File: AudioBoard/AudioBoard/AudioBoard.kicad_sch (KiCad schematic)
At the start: 0 parts

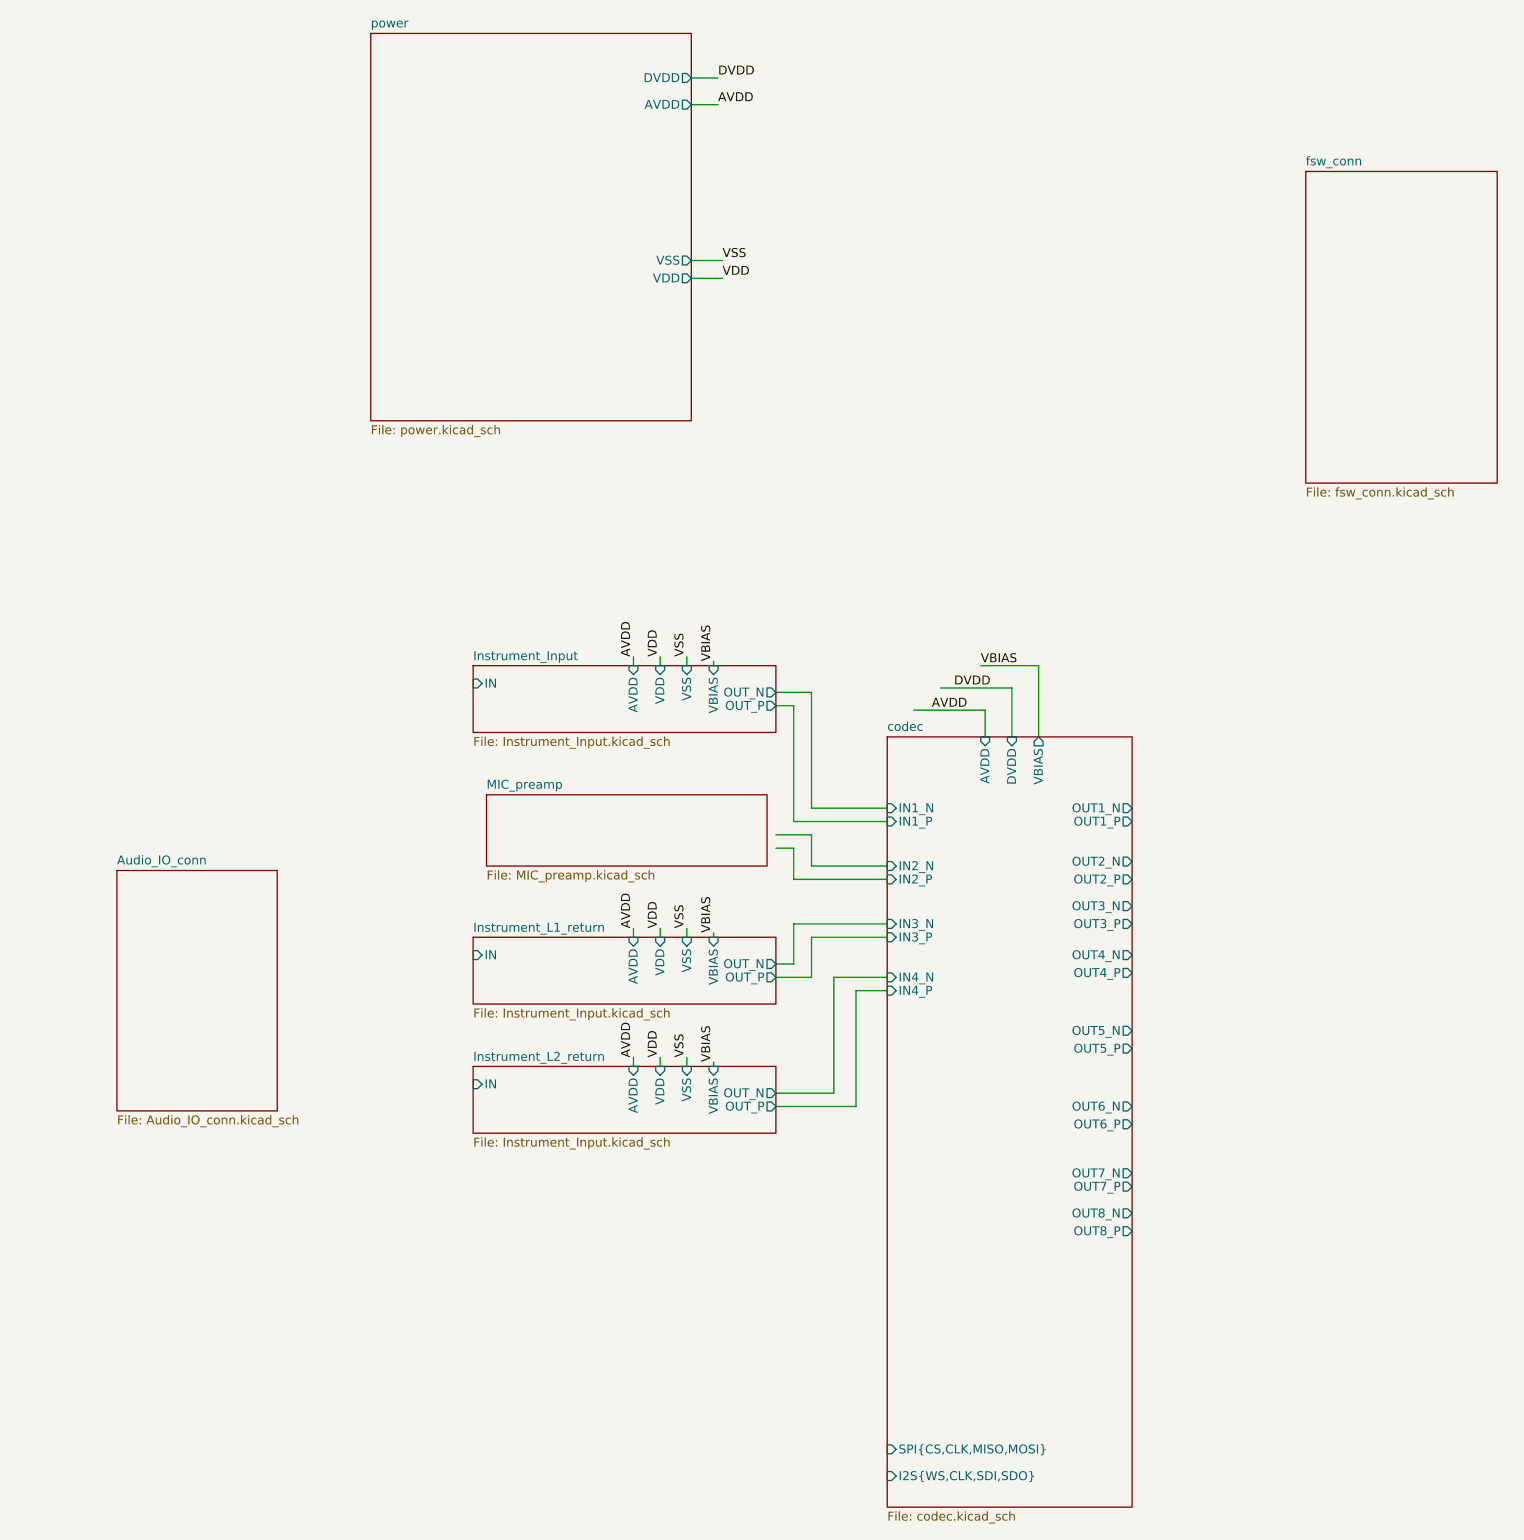
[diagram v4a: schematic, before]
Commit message: added xlr output stage
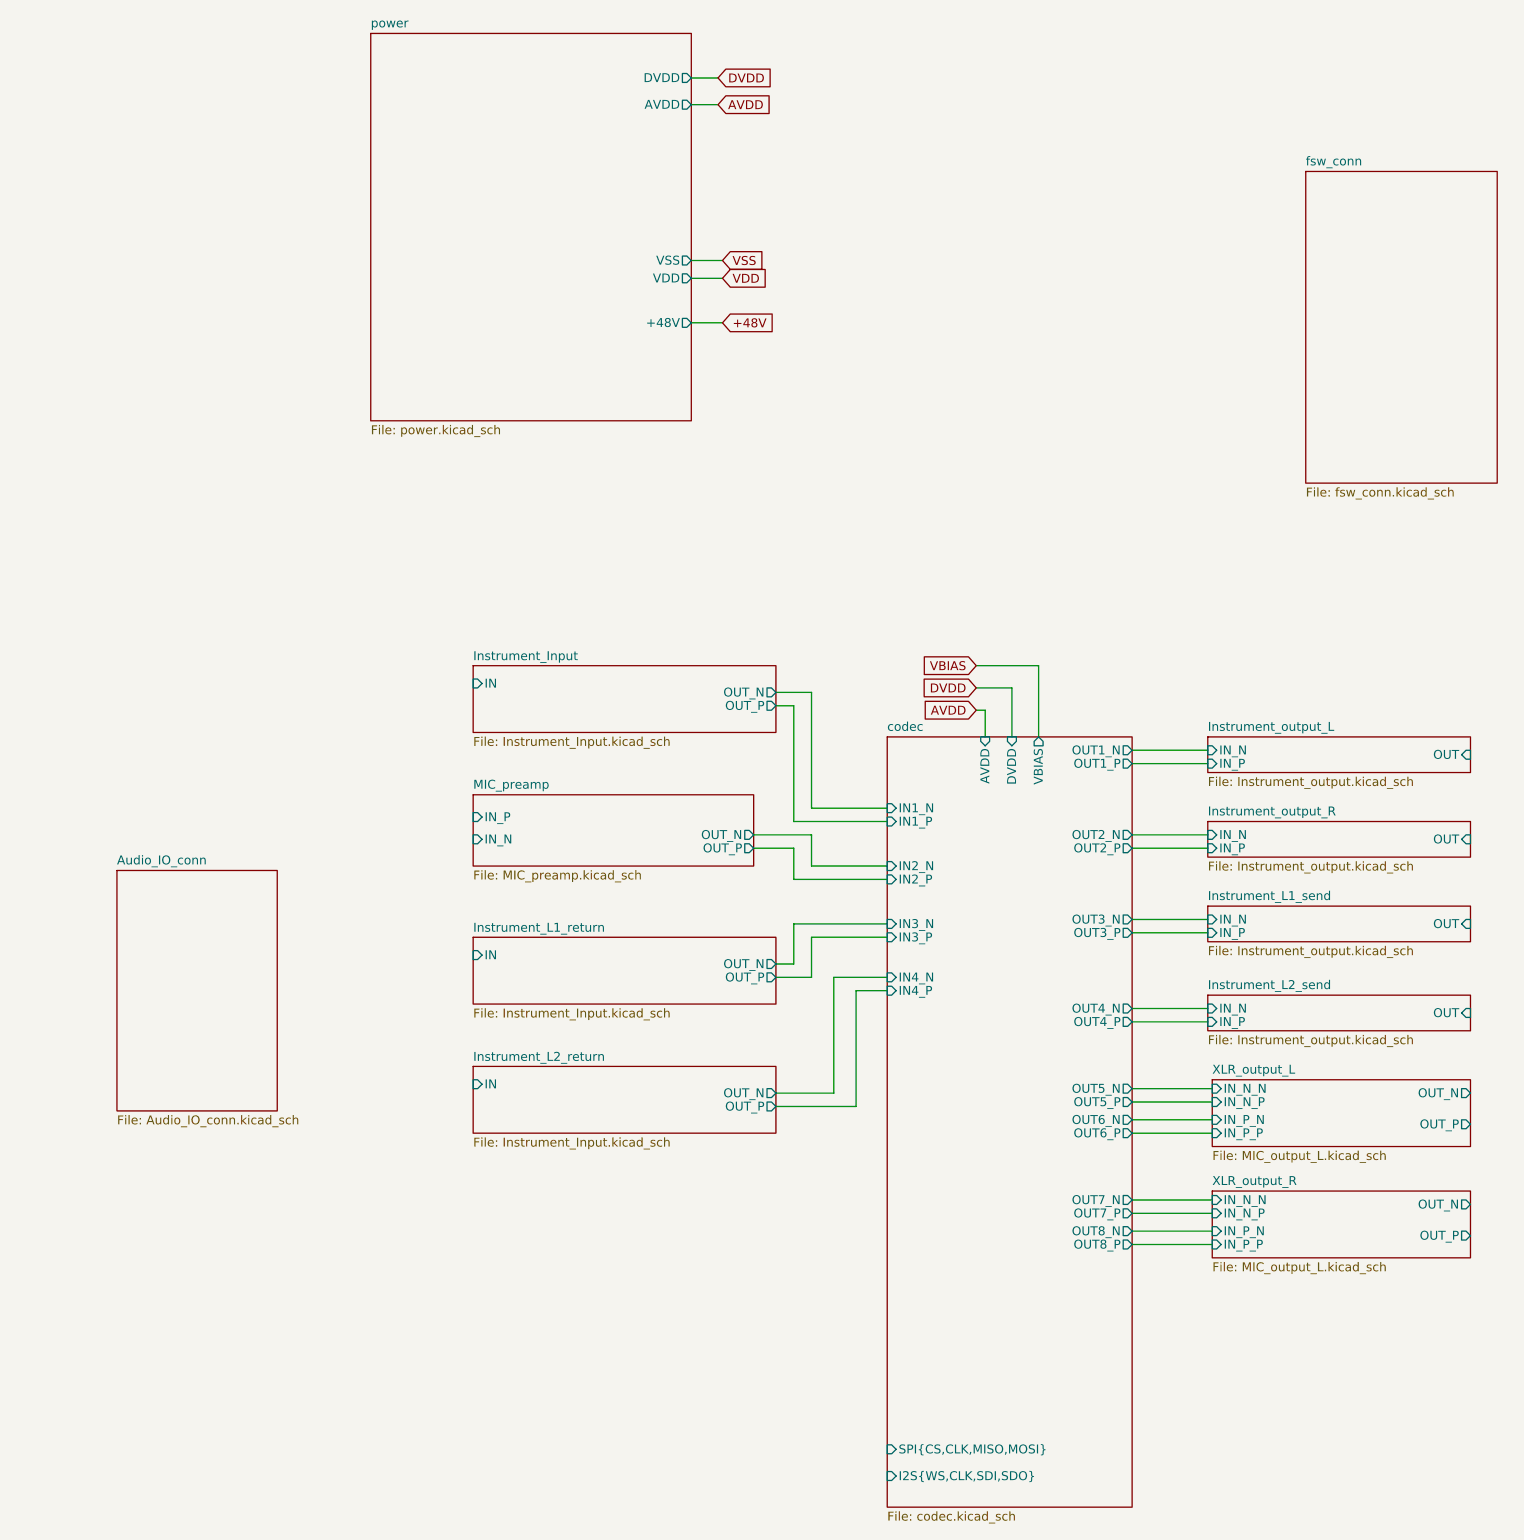
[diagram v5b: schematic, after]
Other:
- added sheet Instrument_L1_send (Instrument_output.kicad_sch)
- added sheet Instrument_L2_send (Instrument_output.kicad_sch)
- added sheet Instrument_output_L (Instrument_output.kicad_sch)
- added sheet Instrument_output_R (Instrument_output.kicad_sch)
- added sheet XLR_output_L (MIC_output_L.kicad_sch)
- added sheet XLR_output_R (MIC_output_L.kicad_sch)
- sheet Instrument_Input ports: added none; removed AVDD, VBIAS, VDD, VSS
- sheet Instrument_L1_return ports: added none; removed AVDD, VBIAS, VDD, VSS
- sheet Instrument_L2_return ports: added none; removed AVDD, VBIAS, VDD, VSS
- sheet MIC_preamp ports: added IN_N, IN_P, OUT_N, OUT_P; removed none
- sheet power ports: added +48V; removed none

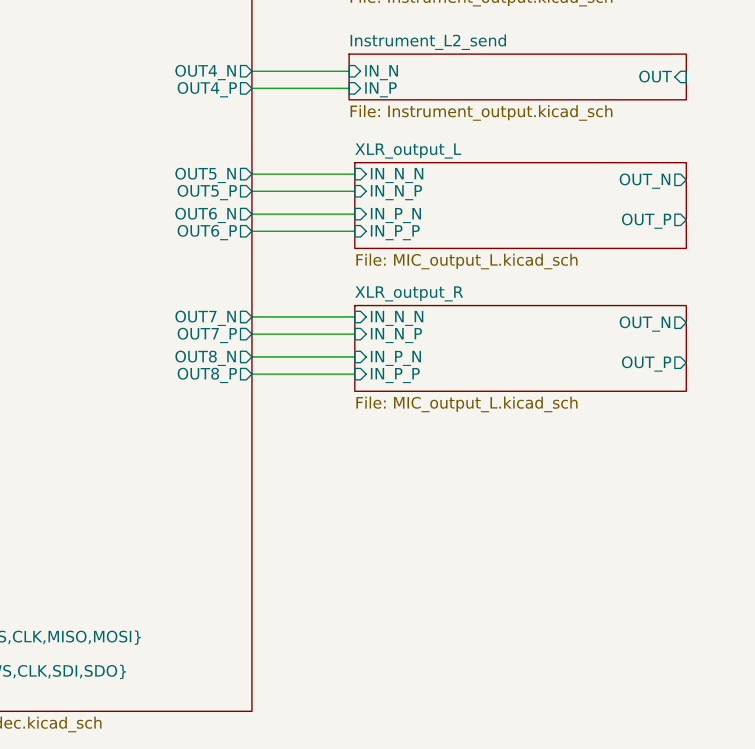
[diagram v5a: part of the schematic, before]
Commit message: added dxf file to pcb view
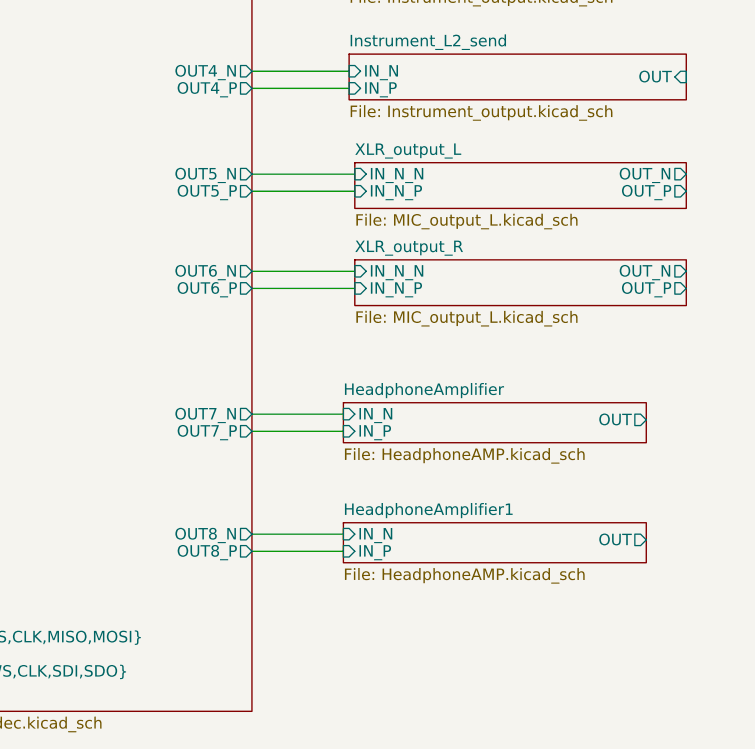
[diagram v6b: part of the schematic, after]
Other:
- added sheet HeadphoneAmplifier (HeadphoneAMP.kicad_sch)
- added sheet HeadphoneAmplifier1 (HeadphoneAMP.kicad_sch)
- sheet XLR_output_L ports: added none; removed IN_P_N, IN_P_P
- sheet XLR_output_R ports: added none; removed IN_P_N, IN_P_P
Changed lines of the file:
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@@
+	(wire
+		(pts
+			(xy 227.965 219.075) (xy 238.125 219.075)
+		)
+		(stroke
+			(width 0)
+			(type default)
+		)
+	)
 	(wire
 		(pts
@@
 	(wire
 		(pts
-			(xy 227.965 210.82) (xy 239.395 210.82)
-		)
-		(stroke
-			(width 0)
-			(type default)
-		)
-	)
-	(wire
-		(pts
 			(xy 179.705 152.4) (xy 193.04 152.4)
 		)
@@
 	(wire
 		(pts
-			(xy 227.965 208.28) (xy 239.395 208.28)
+			(xy 227.965 201.295) (xy 239.395 201.295)
 		)
 		(stroke
@@
 	(wire
 		(pts
+			(xy 227.965 203.2) (xy 239.395 203.2)
+		)
+		(stroke
+			(width 0)
+			(type default)
+		)
+	)
+	(wire
+		(pts
 			(xy 207.01 136.525) (xy 207.01 140.335)
 		)
@@
 	(wire
 		(pts
-			(xy 227.965 196.85) (xy 239.395 196.85)
-		)
-		(stroke
-			(width 0)
-			(type default)
-		)
-	)
-	(wire
-		(pts
 			(xy 193.04 167.005) (xy 179.705 167.005)
 		)
@@
 	(wire
 		(pts
+			(xy 227.965 217.17) (xy 238.125 217.17)
+		)
+		(stroke
+			(width 0)
+			(type default)
+		)
+	)
+	(wire
+		(pts
 			(xy 169.545 72.39) (xy 165.1 72.39)
 		)
@@
 	(wire
 		(pts
+			(xy 227.965 232.41) (xy 238.125 232.41)
+		)
+		(stroke
+			(width 0)
+			(type default)
+		)
+	)
+	(wire
+		(pts
 			(xy 227.965 180.975) (xy 238.76 180.975)
 		)
@@
 	(wire
 		(pts
-			(xy 239.395 194.945) (xy 227.965 194.945)
-		)
-		(stroke
-			(width 0)
-			(type default)
-		)
-	)
-	(wire
-		(pts
 			(xy 227.965 192.405) (xy 239.395 192.405)
 		)
@@
 	(wire
 		(pts
-			(xy 227.965 206.375) (xy 239.395 206.375)
+			(xy 227.965 230.505) (xy 238.125 230.505)
 		)
 		(stroke
@@
 		(pts
 			(xy 173.99 156.21) (xy 179.705 156.21)
-		)
-		(stroke
-			(width 0)
-			(type default)
-		)
-	)
-	(wire
-		(pts
-			(xy 227.965 212.725) (xy 239.395 212.725)
 		)
 		(stroke
@@
 	)
 	(sheet
+		(at 238.125 229.235)
+		(size 33.655 4.445)
+		(exclude_from_sim no)
+		(in_bom yes)
+		(on_board yes)
+		(dnp no)
+		(fields_autoplaced yes)
+		(stroke
+			(width 0.1524)
+			(type solid)
+		)
+		(fill
+			(color 0 0 0 0)
+		)
+		(property "Sheetname" "HeadphoneAmplifier1"
+			(at 238.125 228.5234 0)
+			(show_name no)
+			(do_not_autoplace no)
+			(effects
+				(font
+					(size 1.27 1.27)
+				)
+				(justify left bottom)
+			)
+		)
+		(property "Sheetfile" "HeadphoneAMP.kicad_sch"
+			(at 238.125 234.2646 0)
+			(show_name no)
+			(do_not_autoplace no)
+			(effects
+				(font
+					(size 1.27 1.27)
+				)
+				(justify left top)
+			)
+		)
+		(pin "IN_N" input
+			(at 238.125 230.505 180)
+			(effects
+				(font
+					(size 1.27 1.27)
+				)
+				(justify left)
+			)
+		)
+		(pin "IN_P" input
+			(at 238.125 232.41 180)
+			(effects
+				(font
+					(size 1.27 1.27)
+				)
+				(justify left)
+			)
+		)
+		(pin "OUT" output
+			(at 271.78 231.14 0)
+			(effects
+				(font
+					(size 1.27 1.27)
+				)
+				(justify right)
+			)
+		)
+		(instances
+			(project "AudioBoard"
+				(path "/dd5d876d-fff7-4cb4-baee-a023036d12ae"
+					(page "19")
+				)
+			)
+		)
+	)
+	(sheet
 		(at 238.76 164.465)
 		(size 37.465 5.08)
@@
 	)
 	(sheet
+		(at 238.125 215.9)
+		(size 33.655 4.445)
+		(exclude_from_sim no)
+		(in_bom yes)
+		(on_board yes)
+		(dnp no)
+		(fields_autoplaced yes)
+		(stroke
+			(width 0.1524)
+			(type solid)
+		)
+		(fill
+			(color 0 0 0 0)
+		)
+		(property "Sheetname" "HeadphoneAmplifier"
+			(at 238.125 215.1884 0)
+			(show_name no)
+			(do_not_autoplace no)
+			(effects
+				(font
+					(size 1.27 1.27)
+				)
+				(justify left bottom)
+			)
+		)
+		(property "Sheetfile" "HeadphoneAMP.kicad_sch"
+			(at 238.125 220.9296 0)
+			(show_name no)
+			(do_not_autoplace no)
+			(effects
+				(font
+					(size 1.27 1.27)
+				)
+				(justify left top)
+			)
+		)
+		(pin "IN_N" input
+			(at 238.125 217.17 180)
+			(effects
+				(font
+					(size 1.27 1.27)
+				)
+				(justify left)
+			)
+		)
+		(pin "IN_P" input
+			(at 238.125 219.075 180)
+			(effects
+				(font
+					(size 1.27 1.27)
+				)
+				(justify left)
+			)
+		)
+		(pin "OUT" output
+			(at 271.78 217.805 0)
+			(effects
+				(font
+					(size 1.27 1.27)
+				)
+				(justify right)
+			)
+		)
+		(instances
+			(project "AudioBoard"
+				(path "/dd5d876d-fff7-4cb4-baee-a023036d12ae"
+					(page "17")
+				)
+			)
+		)
+	)
+	(sheet
 		(at 133.985 187.325)
 		(size 43.18 9.525)
@@
 	)
 	(sheet
-		(at 239.395 205.105)
-		(size 36.83 9.525)
+		(at 239.395 200.025)
+		(size 36.83 5.08)
 		(exclude_from_sim no)
 		(in_bom yes)
@@
 		)
 		(property "Sheetname" "XLR_output_R"
-			(at 239.395 204.3934 0)
+			(at 239.395 199.3134 0)
 			(show_name no)
 			(do_not_autoplace no)
@@
 		)
 		(property "Sheetfile" "MIC_output_L.kicad_sch"
-			(at 239.395 215.2146 0)
+			(at 239.395 205.6896 0)
 			(show_name no)
 			(do_not_autoplace no)
@@
 		)
 		(property "Field2" ""
-			(at 239.395 205.105 0)
+			(at 239.395 200.025 0)
 			(hide yes)
 			(show_name no)
@@
 		)
 		(pin "IN_N_N" input
-			(at 239.395 206.375 180)
+			(at 239.395 201.295 180)
 			(effects
 				(font
@@
 		)
 		(pin "IN_N_P" input
-			(at 239.395 208.28 180)
-			(effects
-				(font
-					(size 1.27 1.27)
-				)
-				(justify left)
-			)
-		)
-		(pin "IN_P_N" input
-			(at 239.395 210.82 180)
-			(effects
-				(font
-					(size 1.27 1.27)
-				)
-				(justify left)
-			)
-		)
-		(pin "IN_P_P" input
-			(at 239.395 212.725 180)
+			(at 239.395 203.2 180)
 			(effects
 				(font
@@
 		)
 		(pin "OUT_N" output
-			(at 276.225 207.01 0)
+			(at 276.225 201.295 0)
 			(effects
 				(font
@@
 		)
 		(pin "OUT_P" output
-			(at 276.225 211.455 0)
+			(at 276.225 203.2 0)
 			(effects
 				(font
@@
 	(sheet
 		(at 239.395 189.23)
-		(size 36.83 9.525)
+		(size 36.83 5.08)
 		(exclude_from_sim no)
 		(in_bom yes)
@@
 		)
 		(property "Sheetfile" "MIC_output_L.kicad_sch"
-			(at 239.395 199.3396 0)
+			(at 239.395 194.8946 0)
 			(show_name no)
 			(do_not_autoplace no)
@@
 			)
 		)
-		(pin "IN_P_N" input
-			(at 239.395 194.945 180)
-			(effects
-				(font
-					(size 1.27 1.27)
-				)
-				(justify left)
-			)
-		)
-		(pin "IN_P_P" input
-			(at 239.395 196.85 180)
-			(effects
-				(font
-					(size 1.27 1.27)
-				)
-				(justify left)
-			)
-		)
 		(pin "OUT_N" output
-			(at 276.225 191.135 0)
+			(at 276.225 190.5 0)
 			(effects
 				(font
@@
 		)
 		(pin "OUT_P" output
-			(at 276.225 195.58 0)
+			(at 276.225 192.405 0)
 			(effects
 				(font
@@
 		)
 		(pin "OUT6_N" output
-			(at 227.965 194.945 0)
+			(at 227.965 201.295 0)
 			(effects
 				(font
@@
 		)
 		(pin "OUT6_P" output
-			(at 227.965 196.85 0)
+			(at 227.965 203.2 0)
 			(effects
 				(font
@@
 		)
 		(pin "OUT7_N" output
-			(at 227.965 206.375 0)
+			(at 227.965 217.17 0)
 			(effects
 				(font
@@
 		)
 		(pin "OUT7_P" output
-			(at 227.965 208.28 0)
+			(at 227.965 219.075 0)
 			(effects
 				(font
@@
 		)
 		(pin "OUT8_N" output
-			(at 227.965 210.82 0)
+			(at 227.965 230.505 0)
 			(effects
 				(font
@@
 		)
 		(pin "OUT8_P" output
-			(at 227.965 212.725 0)
-			(effects
-				(font
+			(at 227.965 232.41 0)
+			(effects
+				(font
